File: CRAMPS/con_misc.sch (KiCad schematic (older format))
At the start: 17 parts, among them K201 S1, K202 S2, K203 S3, K204 S4, P1 SERIAL1, P2 I2C-1, P211 I2C-0, P213 AUX-4, P214 AUX-2, P215 AUX-3, P216 SERIAL0, U601 24C512

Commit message: Schematic updates mostly complete Pending pin assignment which will happen based on PCB layout Updated netlist imported to PCB, but placement not started
Signed-off-by: Charles Steinkuehler <charles@steinkuehler.net>
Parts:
- removed P213: AUX-4, symbol CONN_18
- removed P214: AUX-2, symbol CONN_5X2
- added P106: TOUCH, symbol CONN_6
- added Q1, Q2: 2N7002, ~, symbol MOSFET_N
- R1, R2, R211, R212: value NF -> 10k
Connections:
- net labels added: ADC_GND, ADC_VDD, AIN0, AIN1, AIN2, AIN3, E2_DIR, E2_STEP, MISO-5V, MOSI-5V, SCK-5V, SCL-5V, SDA-5V, SERVO1-5V, SERVO2-5V, SERVO3-5V, SERVO4-5V, SPI_CS0-5V, VDD_5V
- net labels removed: A4, A5, A6, A7, AD14, AD15, D23, D25, D27, D29, D31, D32, D33, D35, D37, D39, D41, D43, D45, D47, D49, D50-MISO, D51-MOSI, D52-SCK, MISO, MOSI, SCK, SCL1, SDA1, SERVO1, SERVO2, SERVO3, SERVO4, UART1_RX_LV, UART1_TX_LV, UART2_RX_LV, UART2_TX_LV, UART3_RX_LV, UART3_TX_LV
- wire segments 108 -> 87
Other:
- note added: "1k5 Pull ups on Due\n10k Pull up to 5V keeps current\nunder 3mA per I2C spec."
- note added: "Aux2 - Analog"
- note added: "Level translation per I2C specification 2.1 Section 18"
- note added: "Note: \nSignals shared with\nExt2 and I2C1"
- note added: "Note: \nSignals shared with\nUART1 and I2C1"
- note added: "Note: \nThis serial port is the \nmain serial console"
- note added: "Only I/O indicated with a -5V suffix are 5V tolerant. \nDo not exceed 3.3V on any other signals.\nAnalog signals may not exceed 1.8V"
- note added: "Resistive Touch Screen"
- note added: "WARNING:\nSPI_CS1 is NOT 5V Tolerant!"
- note added: "X+"
- note added: "X-"
- note added: "Y+"
- note added: "Y-"
- note removed: "1k5 Pull ups on Due"
- note removed: "Aux2"
- note removed: "Aux4 - general IO"
- note removed: "Mega: same signals as \nMISO, MOSI & SCK"
- note removed: "Must not have external pullups to 5V if IOREF = 3.3V"
- note removed: "NB: On Arduino Due: IOs on this page are not 5V tolerant. Do not exceed 3.3V."
- note removed: "Need buffered outputs?"
- note removed: "Note: this serial port is shared with\nUSB programming port"
- note removed: "These are free \nfor LCD panel etc"
- note removed: "These are shared with E1 \nand E2 stepper signals"
- note removed: "UART-TTL"
- moved on the sheet: C601, K202, K203, K204, P1, P2, P211, P215, P216, R1, R2, R211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

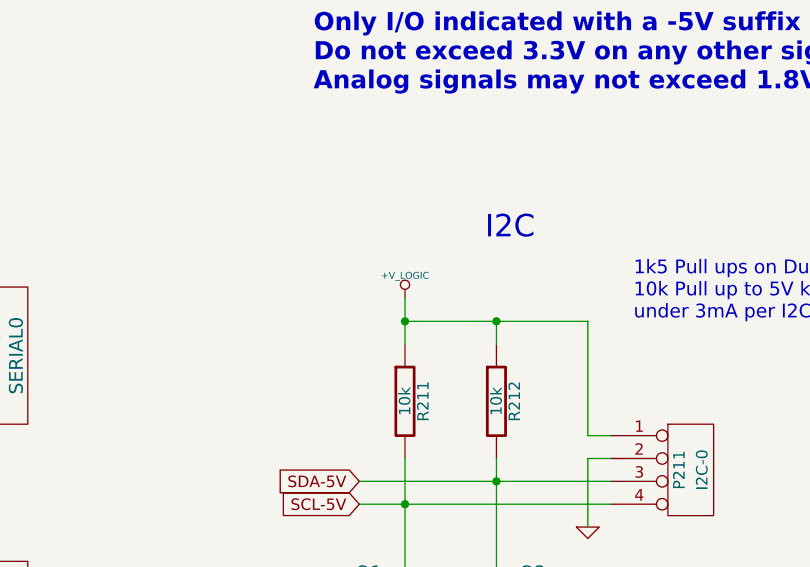
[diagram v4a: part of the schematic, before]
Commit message: Placement complete, tweaking for good results from autorouter
Signed-off-by: Charles Steinkuehler <charles@steinkuehler.net>
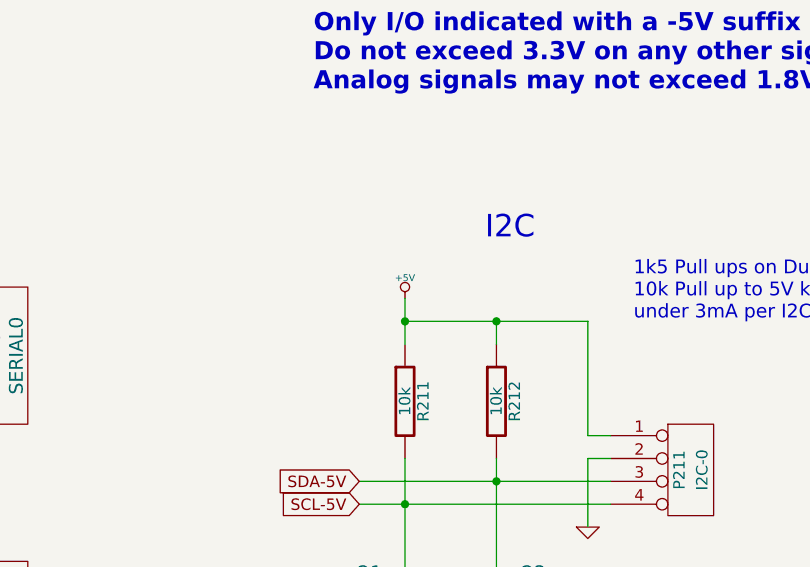
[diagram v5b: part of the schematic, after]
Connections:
- net +5V: now also P211.1 (P1), R211.1, R212.1
- net +V_LOGIC: no longer P211.1 (P1), R211.1, R212.1
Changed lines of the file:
@@
 Sheet 6 10
 Title "CRAMPS (Cape-RAMPS for BeagleBone)"
-Date "8 feb 2014"
+Date "9 feb 2014"
 Rev "v1.0"
 Comp ""
@@
 $EndComp
 $Comp
-L +V_LOGIC #PWR072
-U 1 1 517867C6
-P 4500 1600
-F 0 "#PWR072" H 4500 1570 30  0001 C CNN
-F 1 "+V_LOGIC" H 4500 1700 30  0000 C CNN
-F 2 "" H 4500 1600 60  0001 C CNN
-F 3 "" H 4500 1600 60  0001 C CNN
-	1    4500 1600
-	1    0    0    -1
-$EndComp
-$Comp
-L GND #PWR073
+L GND #PWR072
 U 1 1 5104884C
 P 8400 3900
-F 0 "#PWR073" H 8400 3900 30  0001 C CNN
+F 0 "#PWR072" H 8400 3900 30  0001 C CNN
 F 1 "GND" H 8400 3830 30  0001 C CNN
 F 2 "" H 8400 3900 60  0001 C CNN
@@
 $EndComp
 $Comp
-L GND #PWR074
+L GND #PWR073
 U 1 1 5104861F
 P 2300 2300
-F 0 "#PWR074" H 2300 2300 30  0001 C CNN
+F 0 "#PWR073" H 2300 2300 30  0001 C CNN
 F 1 "GND" H 2300 2230 30  0001 C CNN
 F 2 "" H 2300 2300 60  0001 C CNN
@@
 $EndComp
 $Comp
-L GND #PWR075
+L GND #PWR074
 U 1 1 51047C7E
 P 1550 6500
-F 0 "#PWR075" H 1550 6500 30  0001 C CNN
+F 0 "#PWR074" H 1550 6500 30  0001 C CNN
 F 1 "GND" H 1550 6430 30  0001 C CNN
 F 2 "" H 1550 6500 60  0001 C CNN
@@
 SERVO3-5V
 $Comp
-L GND #PWR076
+L GND #PWR075
 U 1 1 51047C7A
 P 1550 5900
-F 0 "#PWR076" H 1550 5900 30  0001 C CNN
+F 0 "#PWR075" H 1550 5900 30  0001 C CNN
 F 1 "GND" H 1550 5830 30  0001 C CNN
 F 2 "" H 1550 5900 60  0001 C CNN
@@
 $EndComp
 $Comp
-L GND #PWR077
+L GND #PWR076
 U 1 1 51047C77
 P 1550 5300
-F 0 "#PWR077" H 1550 5300 30  0001 C CNN
+F 0 "#PWR076" H 1550 5300 30  0001 C CNN
 F 1 "GND" H 1550 5230 30  0001 C CNN
 F 2 "" H 1550 5300 60  0001 C CNN
@@
 SERVO1-5V
 $Comp
-L GND #PWR078
+L GND #PWR077
 U 1 1 51047C01
 P 1550 4700
-F 0 "#PWR078" H 1550 4700 30  0001 C CNN
+F 0 "#PWR077" H 1550 4700 30  0001 C CNN
 F 1 "GND" H 1550 4630 30  0001 C CNN
 F 2 "" H 1550 4700 60  0001 C CNN
@@
 SDA-5V
 $Comp
-L GND #PWR079
+L GND #PWR078
 U 1 1 51047413
 P 5300 2600
-F 0 "#PWR079" H 5300 2600 30  0001 C CNN
+F 0 "#PWR078" H 5300 2600 30  0001 C CNN
 F 1 "GND" H 5300 2530 30  0001 C CNN
 F 2 "" H 5300 2600 60  0001 C CNN
@@
 	9500 3200 9300 3200
 $Comp
-L +5V #PWR080
+L +5V #PWR079
 U 1 1 52421C84
 P 8400 3100
-F 0 "#PWR080" H 8400 3190 20  0001 C CNN
+F 0 "#PWR079" H 8400 3190 20  0001 C CNN
 F 1 "+5V" H 8400 3190 30  0000 C CNN
 F 2 "" H 8400 3100 60  0000 C CNN
@@
 $EndComp
 $Comp
-L +V_LOGIC #PWR081
+L +V_LOGIC #PWR080
 U 1 1 52475621
 P 9400 3100
-F 0 "#PWR081" H 9400 3070 30  0001 C CNN
+F 0 "#PWR080" H 9400 3070 30  0001 C CNN
 F 1 "+V_LOGIC" H 9400 3200 30  0000 C CNN
 F 2 "" H 9400 3100 60  0001 C CNN
@@
 $EndComp
 $Comp
-L GND #PWR082
+L GND #PWR081
 U 1 1 52B23654
 P 4400 7000
-F 0 "#PWR082" H 4400 7000 30  0001 C CNN
+F 0 "#PWR081" H 4400 7000 30  0001 C CNN
 F 1 "GND" H 4400 6930 30  0001 C CNN
 F 2 "" H 4400 7000 60  0001 C CNN
@@
 Connection ~ 3600 6200
 $Comp
-L +V_LOGIC #PWR083
+L +V_LOGIC #PWR082
 U 1 1 52B2384C
 P 4400 5700
-F 0 "#PWR083" H 4400 5670 30  0001 C CNN
+F 0 "#PWR082" H 4400 5670 30  0001 C CNN
 F 1 "+V_LOGIC" H 4400 5800 30  0000 C CNN
 F 2 "" H 4400 5700 60  0001 C CNN
@@
 $EndComp
 $Comp
-L GND #PWR084
+L GND #PWR083
 U 1 1 52B22346
 P 6000 6600
-F 0 "#PWR084" H 6000 6600 30  0001 C CNN
+F 0 "#PWR083" H 6000 6600 30  0001 C CNN
 F 1 "GND" H 6000 6530 30  0001 C CNN
 F 2 "" H 6000 6600 60  0001 C CNN
@@
 	6000 6500 6000 6600
 $Comp
-L +V_LOGIC #PWR085
+L +V_LOGIC #PWR084
 U 1 1 52B2234D
 P 6000 6000
-F 0 "#PWR085" H 6000 5970 30  0001 C CNN
+F 0 "#PWR084" H 6000 5970 30  0001 C CNN
 F 1 "+V_LOGIC" H 6000 6100 30  0000 C CNN
 F 2 "" H 6000 6000 60  0001 C CNN
@@
 $EndComp
 $Comp
-L +V_LOGIC #PWR086
+L +V_LOGIC #PWR085
 U 1 1 52F04269
 P 4000 2900
-F 0 "#PWR086" H 4000 2870 30  0001 C CNN
+F 0 "#PWR085" H 4000 2870 30  0001 C CNN
 F 1 "+V_LOGIC" H 4000 3000 30  0000 C CNN
 F 2 "" H 4000 2900 60  0001 C CNN
@@
 $EndComp
 $Comp
-L +V_LOGIC #PWR087
+L +V_LOGIC #PWR086
 U 1 1 52F0439C
 P 5400 2900
-F 0 "#PWR087" H 5400 2870 30  0001 C CNN
+F 0 "#PWR086" H 5400 2870 30  0001 C CNN
 F 1 "+V_LOGIC" H 5400 3000 30  0000 C CNN
 F 2 "" H 5400 2900 60  0001 C CNN
@@
 Wire Wire Line
 	8500 3700 8300 3700
+$Comp
+L +5V #PWR087
+U 1 1 52F69B15
+P 4500 1600
+F 0 "#PWR087" H 4500 1690 20  0001 C CNN
+F 1 "+5V" H 4500 1690 30  0000 C CNN
+F 2 "" H 4500 1600 60  0000 C CNN
+F 3 "" H 4500 1600 60  0000 C CNN
+	1    4500 1600
+	1    0    0    -1
+$EndComp
 $EndSCHEMATC

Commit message: Initial BOM files for PCB version 1.0 Added README and ToDo text files
Signed-off-by: Charles Steinkuehler <charles@steinkuehler.net>
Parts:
- C601: Mfg (none) -> Taiyo Yuden; PartNo (none) -> GMK212BJ104KGHT
- K201, K202, K203, K204: Mfg (none) -> Harwin; PartNo (none) -> M20-9990345
- P1, P106, P216: Mfg (none) -> Harwin; PartNo (none) -> M20-9990645
- P2, P211: Mfg (none) -> Harwin; PartNo (none) -> M20-9990445
- P215: Mfg (none) -> Harwin; PartNo (none) -> M20-9980645
- Q1, Q2: Mfg (none) -> Diodes Inc.; PartNo (none) -> 2N7002K-7
- R1, R2, R211, R212: Mfg (none) -> KOA; PartNo (none) -> RK73H2ATTD1002F
- U601: Mfg (none) -> On Semi; PartNo (none) -> CAT24C512WI-GT3
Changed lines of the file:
@@
 Sheet 6 10
 Title "CRAMPS (Cape-RAMPS for BeagleBone)"
-Date "9 feb 2014"
+Date "11 feb 2014"
 Rev "v1.0"
 Comp ""
@@
 F 2 "" H 5750 4750 60  0001 C CNN
 F 3 "" H 5750 4750 60  0001 C CNN
+F 4 "Harwin" H 6250 6550 60  0001 C CNN "Mfg"
+F 5 "M20-9990445" H 6250 6550 60  0001 C CNN "PartNo"
 	1    5750 4750
 	1    0    0    -1
@@
 F 2 "" H 4900 4450 60  0001 C CNN
 F 3 "" H 4900 4450 60  0001 C CNN
+F 4 "KOA" H 6250 6550 60  0001 C CNN "Mfg"
+F 5 "RK73H2ATTD1002F" H 6250 6550 60  0001 C CNN "PartNo"
 	1    4900 4450
 	1    0    0    -1
@@
 F 2 "" H 4500 4450 60  0001 C CNN
 F 3 "" H 4500 4450 60  0001 C CNN
+F 4 "KOA" H 6250 6550 60  0001 C CNN "Mfg"
+F 5 "RK73H2ATTD1002F" H 6250 6550 60  0001 C CNN "PartNo"
 	1    4500 4450
 	1    0    0    -1
@@
 F 2 "" H 2750 3050 60  0001 C CNN
 F 3 "" H 2750 3050 60  0001 C CNN
+F 4 "Harwin" H 6250 6550 60  0001 C CNN "Mfg"
+F 5 "M20-9990645" H 6250 6550 60  0001 C CNN "PartNo"
 	1    2750 3050
 	1    0    0    -1
@@
 F 2 "" H 2750 1850 60  0001 C CNN
 F 3 "" H 2750 1850 60  0001 C CNN
+F 4 "Harwin" H 6250 6550 60  0001 C CNN "Mfg"
+F 5 "M20-9990645" H 6250 6550 60  0001 C CNN "PartNo"
 	1    2750 1850
 	1    0    0    -1
@@
 F 2 "" H 2050 6300 60  0001 C CNN
 F 3 "" H 2050 6300 60  0001 C CNN
+F 4 "Harwin" H 6250 6550 60  0001 C CNN "Mfg"
+F 5 "M20-9990345" H 6250 6550 60  0001 C CNN "PartNo"
 	1    2050 6300
 	1    0    0    1
@@
 F 2 "" H 2050 5700 60  0001 C CNN
 F 3 "" H 2050 5700 60  0001 C CNN
+F 4 "Harwin" H 6250 6550 60  0001 C CNN "Mfg"
+F 5 "M20-9990345" H 6250 6550 60  0001 C CNN "PartNo"
 	1    2050 5700
 	1    0    0    1
@@
 F 2 "" H 2050 5100 60  0001 C CNN
 F 3 "" H 2050 5100 60  0001 C CNN
+F 4 "Harwin" H 6250 6550 60  0001 C CNN "Mfg"
+F 5 "M20-9990345" H 6250 6550 60  0001 C CNN "PartNo"
 	1    2050 5100
 	1    0    0    1
@@
 F 2 "" H 2050 4500 60  0001 C CNN
 F 3 "" H 2050 4500 60  0001 C CNN
+F 4 "Harwin" H 6250 6550 60  0001 C CNN "Mfg"
+F 5 "M20-9990345" H 6250 6550 60  0001 C CNN "PartNo"
 	1    2050 4500
 	1    0    0    1
@@
 F 2 "" H 4500 2050 60  0001 C CNN
 F 3 "" H 4500 2050 60  0001 C CNN
+F 4 "KOA" H 6250 6550 60  0001 C CNN "Mfg"
+F 5 "RK73H2ATTD1002F" H 6250 6550 60  0001 C CNN "PartNo"
 	1    4500 2050
 	1    0    0    -1
@@
 F 2 "" H 4900 2050 60  0001 C CNN
 F 3 "" H 4900 2050 60  0001 C CNN
+F 4 "KOA" H 6250 6550 60  0001 C CNN "Mfg"
+F 5 "RK73H2ATTD1002F" H 6250 6550 60  0001 C CNN "PartNo"
 	1    4900 2050
 	1    0    0    -1
@@
 F 2 "" H 5750 2350 60  0001 C CNN
 F 3 "" H 5750 2350 60  0001 C CNN
+F 4 "Harwin" H 6250 6550 60  0001 C CNN "Mfg"
+F 5 "M20-9990445" H 6250 6550 60  0001 C CNN "PartNo"
 	1    5750 2350
 	1    0    0    -1
@@
 F 2 "" H 8900 3450 60  0000 C CNN
 F 3 "" H 8900 3450 60  0000 C CNN
+F 4 "Harwin" H 6250 6550 60  0001 C CNN "Mfg"
+F 5 "M20-9980645" H 6250 6550 60  0001 C CNN "PartNo"
 	1    8900 3450
 	1    0    0    -1
@@
 F 2 "" H 4400 6300 60  0000 C CNN
 F 3 "" H 4400 6300 60  0000 C CNN
+F 4 "On Semi" H 6250 6550 60  0001 C CNN "Mfg"
+F 5 "CAT24C512WI-GT3" H 6250 6550 60  0001 C CNN "PartNo"
 	1    4400 6300
 	1    0    0    -1
@@
 F 2 "~" H 6038 6150 30  0000 C CNN
 F 3 "~" H 6000 6300 60  0000 C CNN
+F 4 "Taiyo Yuden" H 6250 6550 60  0001 C CNN "Mfg"
+F 5 "GMK212BJ104KGHT" H 6250 6550 60  0001 C CNN "PartNo"
 	1    6000 6300
 	1    0    0    -1
@@
 F 2 "~" H 4400 3000 60  0000 C CNN
 F 3 "~" H 4400 3000 60  0000 C CNN
+F 4 "Diodes Inc." H 6250 6550 60  0001 C CNN "Mfg"
+F 5 "2N7002K-7" H 6250 6550 60  0001 C CNN "PartNo"
 	1    4400 3000
 	1    0    0    -1
@@
 F 2 "~" H 5000 3000 60  0000 C CNN
 F 3 "~" H 5000 3000 60  0000 C CNN
+F 4 "Diodes Inc." H 6250 6550 60  0001 C CNN "Mfg"
+F 5 "2N7002K-7" H 6250 6550 60  0001 C CNN "PartNo"
 	1    5000 3000
 	-1   0    0    -1
@@
 F 2 "" H 9350 1950 60  0001 C CNN
 F 3 "" H 9350 1950 60  0001 C CNN
+F 4 "Harwin" H 6250 6550 60  0001 C CNN "Mfg"
+F 5 "M20-9990645" H 6250 6550 60  0001 C CNN "PartNo"
 	1    9350 1950
 	1    0    0    -1

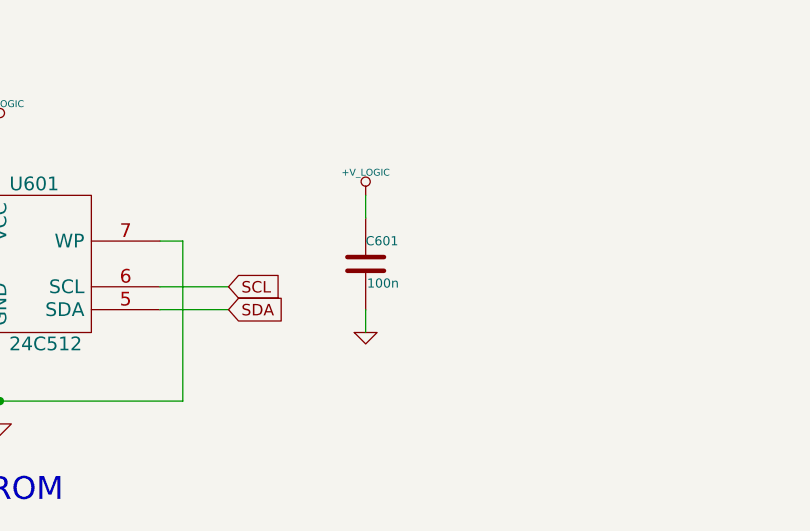
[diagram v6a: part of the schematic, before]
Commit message: BOM Updates Fixed incorrect Molex part number Added Stackpole resistor part numbers Switched to value-sorted BOM export from KiCAD Modified some attribute fields to get same-value parts to list on a single BOM line
Signed-off-by: Charles Steinkuehler <charles@steinkuehler.net>
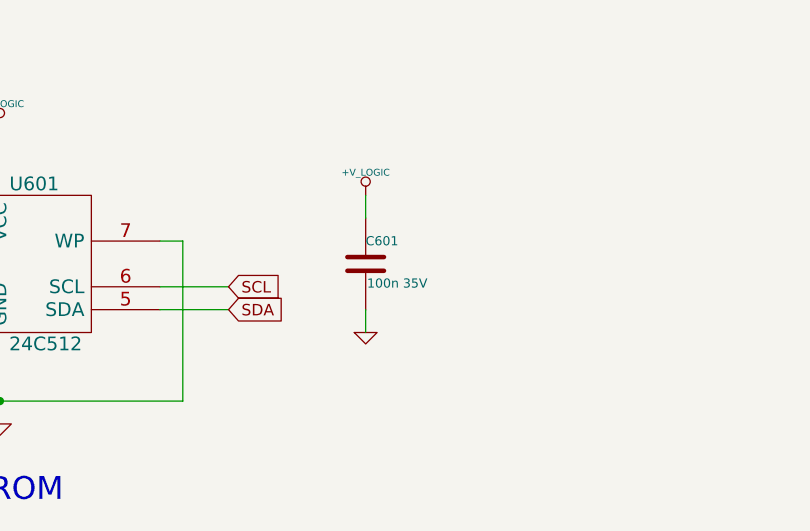
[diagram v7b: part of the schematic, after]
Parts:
- C601: value 100n -> 100n 35V; footprint ~ -> (none)
- R1, R2, R211, R212: AltMfg (none) -> KOA; AltPartNo (none) -> RK73H2ATTD1002F; Mfg KOA -> Stackpole; PartNo RK73H2ATTD1002F -> RMCF0805FT10K0
